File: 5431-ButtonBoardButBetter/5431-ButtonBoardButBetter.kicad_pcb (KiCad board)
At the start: 2 copper layers, 17 parts, among them SW1 SW_DIP_x01, SW10 SW_DIP_x01, SW11 SW_DIP_x01, SW12 SW_DIP_x01, SW13 SW_DIP_x01, SW14 SW_DIP_x01, SW15 SW_DIP_x01, SW16 SW_DIP_x01, SW2 SW_DIP_x01, SW3 SW_DIP_x01, SW4 SW_DIP_x01, SW5 SW_DIP_x01, SW6 SW_DIP_x01, SW7 SW_DIP_x01, SW8 SW_DIP_x01, SW9 SW_DIP_x01, U1 Pico

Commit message: updated layout
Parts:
- added SW17: SW_DIP_x01, Button_Switch_THT:SW_PUSH_6mm, F.Cu at (182.9, 57.1)
- moved SW11 192.5 mm to (256.4, 68.6)
- moved SW6 172.5 mm to (44.5, 86.4)
- moved SW7 151.3 mm to (64.8, 86.4)
- moved SW14 151.1 mm to (236.2, 88.8)
- moved SW8 40.6 mm to (85.1, 86.4)
- moved SW13 40.4 mm to (216.0, 88.8)
- moved SW15 28.6 mm to (256.4, 88.8)
- moved SW10 20.2 mm to (236.2, 68.6)
- moved SW12 20.2 mm to (276.6, 68.6)
- moved SW9 20.2 mm to (216.0, 68.6)
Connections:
- U1 pad 11: Sw9 -> unconnected-(U1-GPIO8-Pad11)
- U1 pad 12: Sw10 -> unconnected-(U1-GPIO9-Pad12)
- U1 pad 14: Sw11 -> unconnected-(U1-GPIO10-Pad14)
- U1 pad 15: Sw12 -> unconnected-(U1-GPIO11-Pad15)
- U1 pad 16: Sw13 -> unconnected-(U1-GPIO12-Pad16)
- U1 pad 17: Sw14 -> unconnected-(U1-GPIO13-Pad17)
- U1 pad 20: unconnected-(U1-GPIO15-Pad20) -> Sw16
- U1 pad 21: unconnected-(U1-GPIO16-Pad21) -> Sw15
- U1 pad 22: unconnected-(U1-GPIO17-Pad22) -> Sw14
- U1 pad 24: unconnected-(U1-GPIO18-Pad24) -> Sw13
- U1 pad 25: unconnected-(U1-GPIO19-Pad25) -> Sw12
- U1 pad 26: unconnected-(U1-GPIO20-Pad26) -> Sw11
- U1 pad 27: unconnected-(U1-GPIO21-Pad27) -> Sw10
- U1 pad 29: unconnected-(U1-GPIO22-Pad29) -> Sw9

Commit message: added slider
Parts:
- added RV1: R_Potentiometer_US, Potentiometer_THT:Potentiometer_Bourns_PTA4543_Single_Slide, F.Cu at (83.7, 29.8)
- added RV2: R_Potentiometer_US, Potentiometer_THT:Potentiometer_Bourns_PTA4543_Single_Slide, F.Cu at (125.3, 64.4)
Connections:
- U1 pad 36: unconnected-(U1-3V3-Pad36) -> +3V3
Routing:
- net GND: track 0.00 -> 102.9 mm

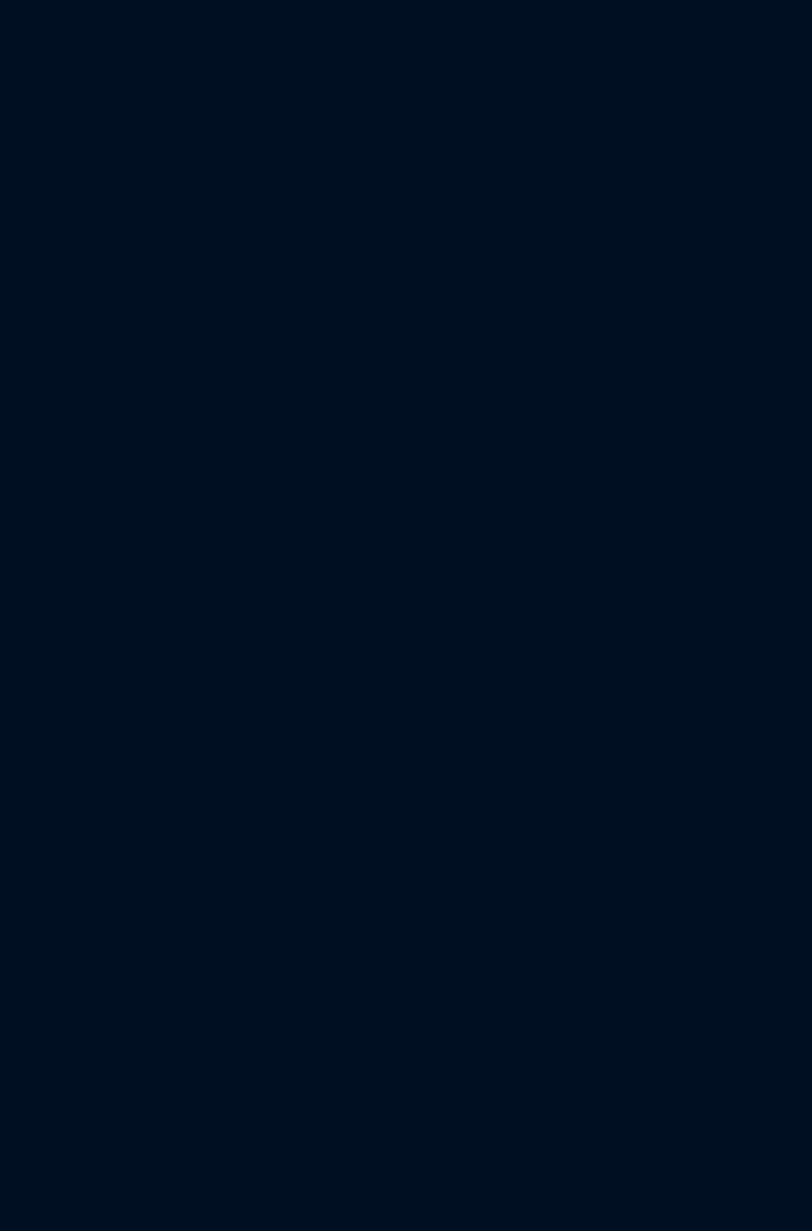
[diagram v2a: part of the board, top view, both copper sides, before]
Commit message: added IC footprint-ish
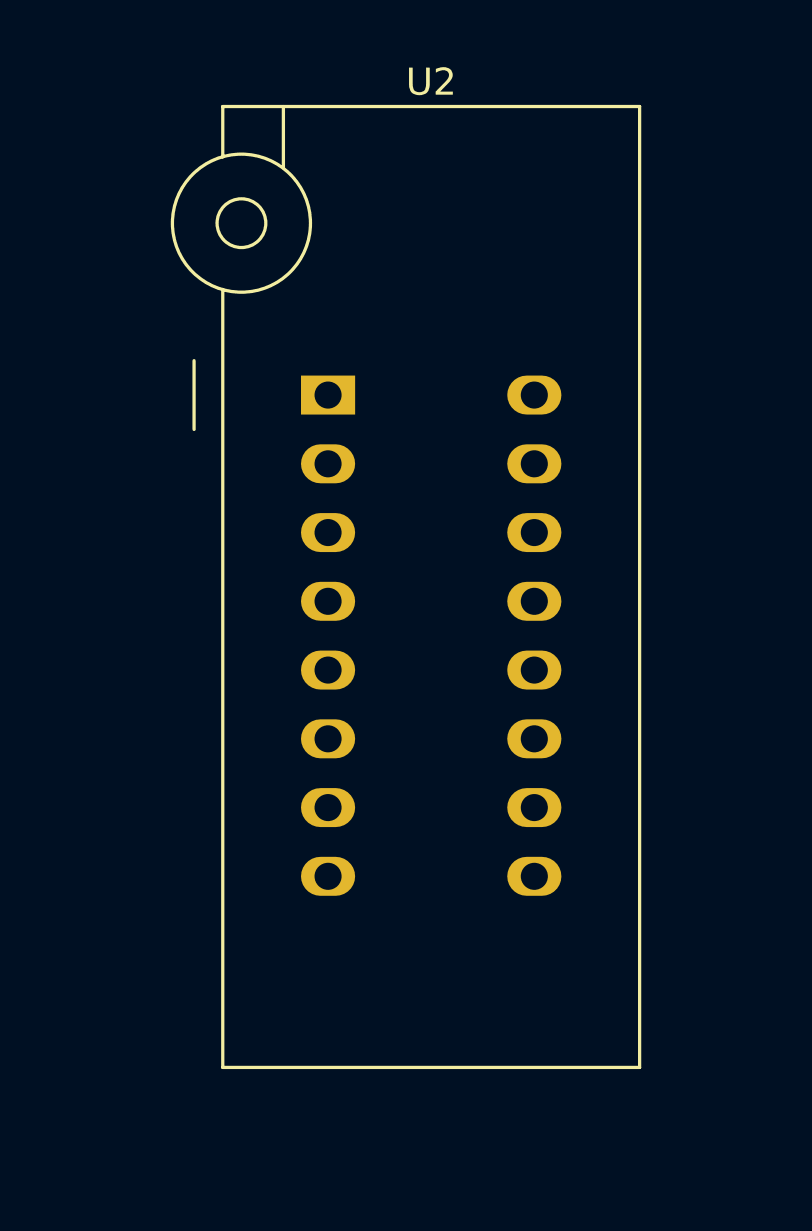
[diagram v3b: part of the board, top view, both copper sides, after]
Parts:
- added U2: MCP3008, Socket:DIP_Socket-16_W4.3_W5.08_W7.62_W10.16_W10.9_3M_216-3340-00-0602J, F.Cu at (162.6, 29.2)
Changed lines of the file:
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@@
   (net 37 "Sw15")
   (net 38 "Sw16")
+  (net 39 "unconnected-(U2-CH2-Pad3)")
+  (net 40 "unconnected-(U2-CH3-Pad4)")
+  (net 41 "unconnected-(U2-CH4-Pad5)")
+  (net 42 "unconnected-(U2-CH5-Pad6)")
+  (net 43 "unconnected-(U2-CH6-Pad7)")
+  (net 44 "unconnected-(U2-CH7-Pad8)")
+  (net 45 "unconnected-(U2-DGND-Pad9)")
+  (net 46 "unconnected-(U2-~{CS}{slash}SHDN-Pad10)")
+  (net 47 "unconnected-(U2-Din-Pad11)")
+  (net 48 "unconnected-(U2-Dout-Pad12)")
+  (net 49 "unconnected-(U2-CLK-Pad13)")
+  (net 50 "unconnected-(U2-AGND-Pad14)")
+  (net 51 "unconnected-(U2-Vref-Pad15)")
+  (net 52 "unconnected-(U2-Vdd-Pad16)")
   (footprint "Button_Switch_Keyboard:SW_Cherry_MX_1.00u_PCB" (layer "F.Cu")
     (at 85.09 86.36)
@@
       (offset (xyz 0 0 0))
       (scale (xyz 1 1 1))
+      (rotate (xyz 0 0 0))
+    )
+  )
+  (footprint "Socket:DIP_Socket-16_W4.3_W5.08_W7.62_W10.16_W10.9_3M_216-3340-00-0602J" (layer "F.Cu")
+    (at 162.56 29.21)
+    (descr "3M 16-pin zero insertion force socket, through-hole, row spacing 7.62 mm (300 mils), http://multimedia.3m.com/mws/media/494546O/3mtm-dip-sockets-100-2-54-mm-ts0365.pdf")
+    (tags "THT DIP DIL ZIF 7.62mm 300mil Socket")
+    (property "Sheetfile" "5431-ButtonBoardButBetter.kicad_sch")
+    (property "Sheetname" "")
+    (property "ki_description" "A/D Converter, 10-Bit, 8-Channel, SPI Interface , 2.7V-5.5V")
+    (property "ki_keywords" "12bit ADC Reference Single Supply SPI 8CH")
+    (attr through_hole)
+    (fp_text reference "U2" (at 3.81 -11.56) (layer "F.SilkS")
+        (effects (font (size 1 1) (thickness 0.15)))
+    )
+    (fp_text value "MCP3008" (at 3.81 25.74) (layer "F.Fab")
+        (effects (font (size 0.6 0.6) (thickness 0.09)))
+    )
+    (fp_text user "${REFERENCE}" (at 3.81 7.09) (layer "F.Fab")
+        (effects (font (size 1 1) (thickness 0.15)))
+    )
+    (fp_line (start -4.95 1.27) (end -4.95 -1.27)
+      (stroke (width 0.12) (type solid)) (layer "F.SilkS"))
+    (fp_line (start -3.89 -10.66) (end -3.89 -8.8)
+      (stroke (width 0.12) (type solid)) (layer "F.SilkS"))
+    (fp_line (start -3.89 -3.9) (end -3.89 24.84)
+      (stroke (width 0.12) (type solid)) (layer "F.SilkS"))
+    (fp_line (start -3.89 24.84) (end 11.51 24.84)
+      (stroke (width 0.12) (type solid)) (layer "F.SilkS"))
+    (fp_line (start -1.65 -10.66) (end -1.65 -8.4)
+      (stroke (width 0.12) (type solid)) (layer "F.SilkS"))
+    (fp_line (start 11.51 -10.66) (end -3.89 -10.66)
+      (stroke (width 0.12) (type solid)) (layer "F.SilkS"))
+    (fp_line (start 11.51 24.84) (end 11.51 -10.66)
+      (stroke (width 0.12) (type solid)) (layer "F.SilkS"))
+    (fp_circle (center -3.2 -6.35) (end -2.3 -6.35)
+      (stroke (width 0.12) (type solid)) (fill none) (layer "F.SilkS"))
+    (fp_circle (center -3.2 -6.35) (end -0.65 -6.35)
+      (stroke (width 0.12) (type solid)) (fill none) (layer "F.SilkS"))
+    (fp_line (start -5.5 -23.36) (end 0.1 -23.36)
+      (stroke (width 0.05) (type solid)) (layer "F.CrtYd"))
+    (fp_line (start -5.5 -3.4) (end -5.5 -23.36)
+      (stroke (width 0.05) (type solid)) (layer "F.CrtYd"))
+    (fp_line (start -4.29 -3.4) (end -5.5 -3.4)
+      (stroke (width 0.05) (type solid)) (layer "F.CrtYd"))
+    (fp_line (start -4.29 25.24) (end -4.29 -3.4)
+      (stroke (width 0.05) (type solid)) (layer "F.CrtYd"))
+    (fp_line (start 0.1 -23.36) (end 0.1 -11.06)
+      (stroke (width 0.05) (type solid)) (layer "F.CrtYd"))
+    (fp_line (start 0.1 -11.06) (end 11.91 -11.06)
+      (stroke (width 0.05) (type solid)) (layer "F.CrtYd"))
+    (fp_line (start 11.91 -11.06) (end 11.91 25.24)
+      (stroke (width 0.05) (type solid)) (layer "F.CrtYd"))
+    (fp_line (start 11.91 25.24) (end -4.29 25.24)
+      (stroke (width 0.05) (type solid)) (layer "F.CrtYd"))
+    (fp_line (start -5 -21.46) (end -5 -17.86)
+      (stroke (width 0.1) (type solid)) (layer "F.Fab"))
+    (fp_line (start -5 -21.46) (end -3.7 -22.86)
+      (stroke (width 0.1) (type solid)) (layer "F.Fab"))
+    (fp_line (start -5 -17.86) (end -3.5 -15.86)
+      (stroke (width 0.1) (type solid)) (layer "F.Fab"))
+    (fp_line (start -5 -17.86) (end -0.4 -17.86)
+      (stroke (width 0.1) (type solid)) (layer "F.Fab"))
+    (fp_line (start -3.79 -9.4) (end -2.85 -10.56)
+      (stroke (width 0.1) (type solid)) (layer "F.Fab"))
+    (fp_line (start -3.79 24.74) (end -3.79 -9.4)
+      (stroke (width 0.1) (type solid)) (layer "F.Fab"))
+    (fp_line (start -3.7 -22.86) (end -1.7 -22.86)
+      (stroke (width 0.1) (type solid)) (layer "F.Fab"))
+    (fp_line (start -3.5 -15.86) (end -1.9 -15.86)
+      (stroke (width 0.1) (type solid)) (layer "F.Fab"))
+    (fp_line (start -3.5 -9.75) (end -3.5 -15.86)
+      (stroke (width 0.1) (type solid)) (layer "F.Fab"))
+    (fp_line (start -2.85 -10.56) (end 11.41 -10.56)
+      (stroke (width 0.1) (type solid)) (layer "F.Fab"))
+    (fp_line (start -1.9 -15.86) (end -1.9 -10.56)
+      (stroke (width 0.1) (type solid)) (layer "F.Fab"))
+    (fp_line (start -1.7 -22.86) (end -0.4 -21.46)
+      (stroke (width 0.1) (type solid)) (layer "F.Fab"))
+    (fp_line (start -0.4 -21.46) (end -5 -21.46)
+      (stroke (width 0.1) (type solid)) (layer "F.Fab"))
+    (fp_line (start -0.4 -17.86) (end -1.9 -15.86)
+      (stroke (width 0.1) (type solid)) (layer "F.Fab"))
+    (fp_line (start -0.4 -17.86) (end -0.4 -21.46)
+      (stroke (width 0.1) (type solid)) (layer "F.Fab"))
+    (fp_line (start 11.41 -10.56) (end 11.41 24.74)
+      (stroke (width 0.1) (type solid)) (layer "F.Fab"))
+    (fp_line (start 11.41 24.74) (end -3.79 24.74)
+      (stroke (width 0.1) (type solid)) (layer "F.Fab"))
+    (pad "1" thru_hole rect (at 0 0) (size 2 1.44) (drill 1) (layers "*.Cu" "*.Mask")
+      (net 24 "Net-(U2-CH0)") (pinfunction "CH0") (pintype "input"))
+    (pad "2" thru_hole oval (at 0 2.54) (size 2 1.44) (drill 1) (layers "*.Cu" "*.Mask")
+      (net 31 "Net-(U2-CH1)") (pinfunction "CH1") (pintype "input"))
+    (pad "3" thru_hole oval (at 0 5.08) (size 2 1.44) (drill 1) (layers "*.Cu" "*.Mask")
+      (net 39 "unconnected-(U2-CH2-Pad3)") (pinfunction "CH2") (pintype "input"))
+    (pad "4" thru_hole oval (at 0 7.62) (size 2 1.44) (drill 1) (layers "*.Cu" "*.Mask")
+      (net 40 "unconnected-(U2-CH3-Pad4)") (pinfunction "CH3") (pintype "input"))
+    (pad "5" thru_hole oval (at 0 10.16) (size 2 1.44) (drill 1) (layers "*.Cu" "*.Mask")
+      (net 41 "unconnected-(U2-CH4-Pad5)") (pinfunction "CH4") (pintype "input"))
+    (pad "6" thru_hole oval (at 0 12.7) (size 2 1.44) (drill 1) (layers "*.Cu" "*.Mask")
+      (net 42 "unconnected-(U2-CH5-Pad6)") (pinfunction "CH5") (pintype "input"))
+    (pad "7" thru_hole oval (at 0 15.24) (size 2 1.44) (drill 1) (layers "*.Cu" "*.Mask")
+      (net 43 "unconnected-(U2-CH6-Pad7)") (pinfunction "CH6") (pintype "input"))
+    (pad "8" thru_hole oval (at 0 17.78) (size 2 1.44) (drill 1) (layers "*.Cu" "*.Mask")
+      (net 44 "unconnected-(U2-CH7-Pad8)") (pinfunction "CH7") (pintype "input"))
+    (pad "9" thru_hole oval (at 7.62 17.78) (size 2 1.44) (drill 1) (layers "*.Cu" "*.Mask")
+      (net 45 "unconnected-(U2-DGND-Pad9)") (pinfunction "DGND") (pintype "power_in"))
+    (pad "10" thru_hole oval (at 7.62 15.24) (size 2 1.44) (drill 1) (layers "*.Cu" "*.Mask")
+      (net 46 "unconnected-(U2-~{CS}{slash}SHDN-Pad10)") (pinfunction "~{CS}/SHDN") (pintype "input"))
+    (pad "11" thru_hole oval (at 7.62 12.7) (size 2 1.44) (drill 1) (layers "*.Cu" "*.Mask")
+      (net 47 "unconnected-(U2-Din-Pad11)") (pinfunction "Din") (pintype "input"))
+    (pad "12" thru_hole oval (at 7.62 10.16) (size 2 1.44) (drill 1) (layers "*.Cu" "*.Mask")
+      (net 48 "unconnected-(U2-Dout-Pad12)") (pinfunction "Dout") (pintype "output"))
+    (pad "13" thru_hole oval (at 7.62 7.62) (size 2 1.44) (drill 1) (layers "*.Cu" "*.Mask")
+      (net 49 "unconnected-(U2-CLK-Pad13)") (pinfunction "CLK") (pintype "input"))
+    (pad "14" thru_hole oval (at 7.62 5.08) (size 2 1.44) (drill 1) (layers "*.Cu" "*.Mask")
+      (net 50 "unconnected-(U2-AGND-Pad14)") (pinfunction "AGND") (pintype "power_in"))
+    (pad "15" thru_hole oval (at 7.62 2.54) (size 2 1.44) (drill 1) (layers "*.Cu" "*.Mask")
+      (net 51 "unconnected-(U2-Vref-Pad15)") (pinfunction "Vref") (pintype "power_in"))
+    (pad "16" thru_hole oval (at 7.62 0) (size 2 1.44) (drill 1) (layers "*.Cu" "*.Mask")
+      (net 52 "unconnected-(U2-Vdd-Pad16)") (pinfunction "Vdd") (pintype "power_in"))
+    (model "${KICAD6_3DMODEL_DIR}/Socket.3dshapes/DIP_Socket-16_W4.3_W5.08_W7.62_W10.16_W10.9_3M_216-3340-00-0602J.wrl"
+      (offset (xyz 0 0 0))
+      (scale (xyz 1 1 1))

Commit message: done with parts
all parts added, need to place, define edge, and wire
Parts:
- removed SW4, SW9: SW_DIP_x01, Button_Switch_Keyboard:SW_Cherry_MX_1.00u_PCB
- added U3: COM-09032, COM-09032:XDCR_COM-09032, F.Cu at (172.7, 53.3)
- added U4: COM-09032, COM-09032:XDCR_COM-09032, F.Cu at (114.3, 53.3)
- moved RV1 134.7 mm to (218.4, 29.2), turned to -90 degrees
- moved U2 126.8 mm to (153.3, 155.7), turned to -90 degrees
- moved RV2 51.4 mm to (82.6, 35.8)
- moved SW1 39.5 mm to (27.9, 105.4), turned to 25 degrees
- moved SW5 39.4 mm to (36.5, 123.8), turned to 25 degrees
- moved SW12 34.7 mm to (274.7, 103.2), turned to -25 degrees
- moved SW16 34.3 mm to (266.2, 121.5), turned to -25 degrees
- moved SW17 33.4 mm to (180.9, 90.5)
- moved SW2 30.8 mm to (46.4, 96.8), turned to 25 degrees
- moved SW6 30.7 mm to (54.9, 115.2), turned to 25 degrees
- moved SW11 26.1 mm to (256.4, 94.7), turned to -25 degrees
- moved SW15 25.7 mm to (247.8, 113.0), turned to -25 degrees
- moved U1 25.2 mm to (146.1, 112.0)
- moved SW3 22.2 mm to (64.8, 88.2), turned to 25 degrees
- moved SW7 22.0 mm to (73.4, 106.6), turned to 25 degrees
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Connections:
- U2 pad 3: unconnected-(U2-CH2-Pad3) -> VRx1
- U2 pad 4: unconnected-(U2-CH3-Pad4) -> VRy1
- U2 pad 5: unconnected-(U2-CH4-Pad5) -> VRx2
- U2 pad 6: unconnected-(U2-CH5-Pad6) -> VRy2
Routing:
- net GND: track 102.9 -> 0.00 mm
- net unconnected-(U2-CH7-Pad8): vias 0 -> 3

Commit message: linked mux to pico
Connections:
- U1 pad 14: unconnected-(U1-GPIO10-Pad14) -> Sw10
- U1 pad 15: unconnected-(U1-GPIO11-Pad15) -> Sw11
- U1 pad 16: unconnected-(U1-GPIO12-Pad16) -> Sw12
- U1 pad 17: unconnected-(U1-GPIO13-Pad17) -> Sw14
- U1 pad 19: unconnected-(U1-GPIO14-Pad19) -> Sw15
- U1 pad 21: Sw15 -> Sw13
- U1 pad 22: Sw14 -> Sw9
- U1 pad 24: Sw13 -> CLK
- U1 pad 25: Sw12 -> Dout
- U1 pad 26: Sw11 -> Din
- U1 pad 27: Sw10 -> CS
- U1 pad 29: Sw9 -> unconnected-(U1-GPIO22-Pad29)
- U2 pad 10: unconnected-(U2-~{CS}/SHDN-Pad10) -> CS
- U2 pad 11: unconnected-(U2-Din-Pad11) -> Din
- U2 pad 12: unconnected-(U2-Dout-Pad12) -> Dout
- U2 pad 13: unconnected-(U2-CLK-Pad13) -> CLK
- U2 pad 14: unconnected-(U2-AGND-Pad14) -> GND
- U2 pad 15: unconnected-(U2-Vref-Pad15) -> +3V3
- U2 pad 16: unconnected-(U2-Vdd-Pad16) -> +3V3
- U2 pad 9: unconnected-(U2-DGND-Pad9) -> GND

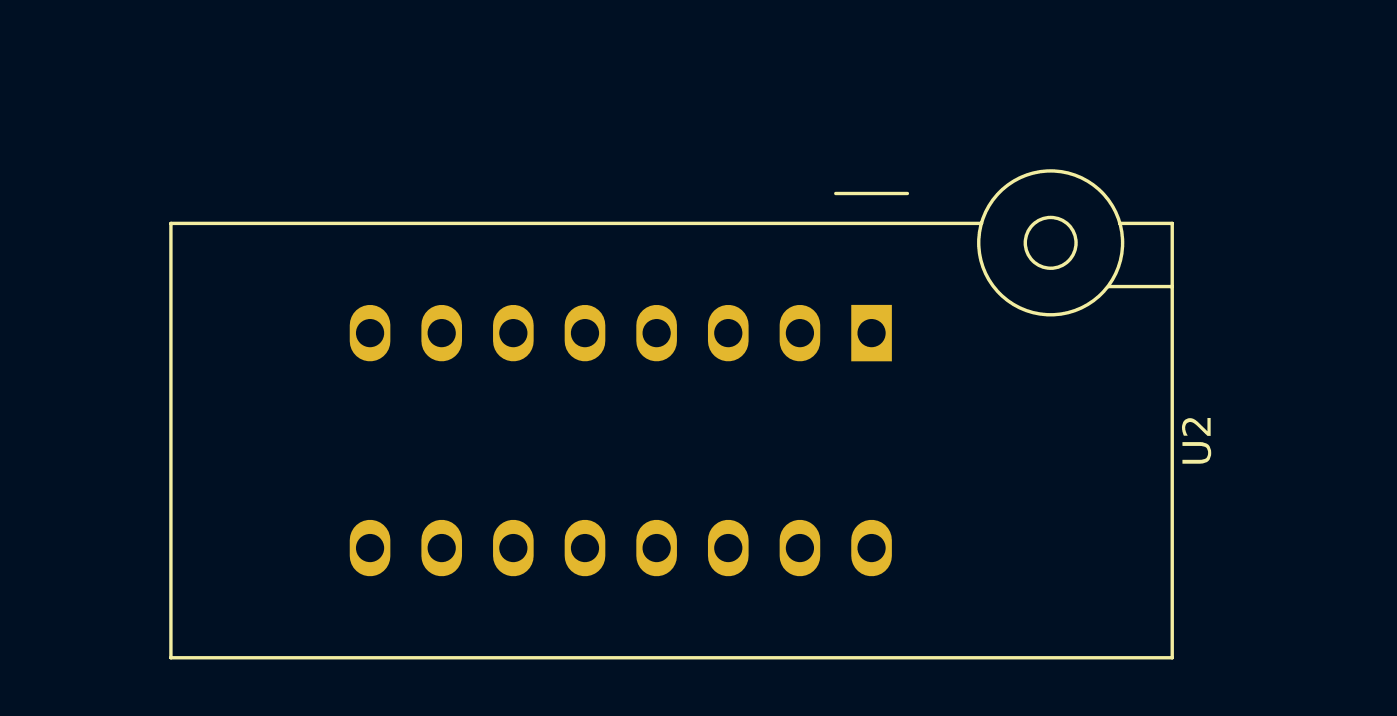
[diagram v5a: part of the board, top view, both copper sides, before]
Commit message: better IC footprint
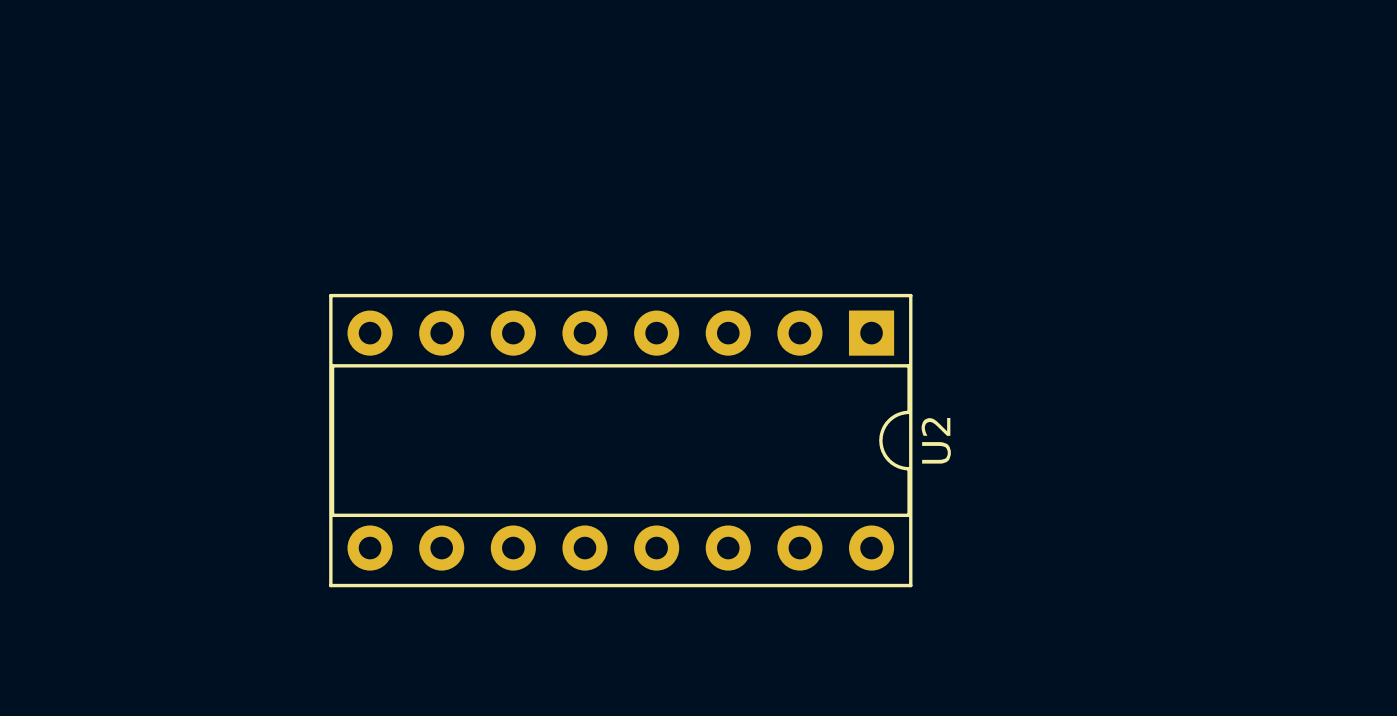
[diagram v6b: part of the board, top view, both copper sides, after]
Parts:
- U2: footprint Socket:DIP_Socket-16_W4.3_W5.08_W7.62_W10.16_W10.9_3M_216-3340-00-0602J -> Package_DIP:DIP-16_W7.62mm_Socket

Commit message: final layout
edge cuts and traces left
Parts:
- moved RV1 101.2 mm to (126.4, 71.2)
- moved RV2 96.5 mm to (172.4, 71.2)
- moved SW17 63.3 mm to (144.4, 142.1)
- moved U3 45.5 mm to (190.6, 95.2), turned to 0 degrees
- moved U4 43.0 mm to (104.6, 95.2), turned to 0 degrees
- moved SW13 23.3 mm to (198.2, 115.1), turned to 0 degrees
- moved U2 23.2 mm to (138.7, 137.7), turned to 90 degrees
- moved SW10 21.8 mm to (218.2, 95.1), turned to 0 degrees
- moved SW8 20.0 mm to (102.2, 115.1), turned to 0 degrees
- moved SW3 18.7 mm to (82.2, 95.1), turned to 0 degrees
- moved SW12 18.4 mm to (258.2, 95.1), turned to 0 degrees
- moved SW11 18.2 mm to (238.2, 95.1), turned to 0 degrees
- moved SW1 17.6 mm to (42.2, 95.1), turned to 0 degrees
- moved SW2 15.9 mm to (62.2, 95.1), turned to 0 degrees
- moved SW14 15.6 mm to (218.2, 115.1), turned to 0 degrees
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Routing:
- net unconnected-(U2-CH7-Pad8): vias 3 -> 0
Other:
- board outline added: 238.1 x 84.3 mm
- board text removed: "Designed by Cyrus Lauderdale"
